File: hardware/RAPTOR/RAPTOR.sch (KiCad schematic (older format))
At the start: 45 parts, among them J1 SOLC_CONN, J2 SOLP_CONN, J3 JST_2MM_MALE, J4 CONN_LED_FIX, J5 CONN_SOLP_LED, J6 CONN_SOLC_LED, P1 Power, P2 Analog, P3 Digital, P4 Digital, P5 CONN_01X01, P6 CONN_01X01, P7 CONN_01X01, P8 CONN_01X01, Q1 MOSFET-NCH-2N7002PW, Q2 MOSFET-NCH-2N7002PW, Q3 MOSFET-NCH-2N7002PW, Q4 MOSFET-NCH-2N7002PW, SW1 EEPROM_BTN, SW2 SOLC_SW, SW3 SOLP_SW, U1 BMP280 Breakout, U2 BNO055 Breakout, U3 OpenLog, U4 AdafruitGPS, U5 U3V12F12, U6 L7805

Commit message: moved a single mosfet
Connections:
- wire segments 157 -> 158
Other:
- moved on the sheet: Q1
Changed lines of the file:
@@
 L RAPTOR-rescue:MOSFET-NCH-2N7002PW-SparkFun-DiscreteSemi Q1
 U 1 1 5BE8A581
-P 4850 2400
-F 0 "Q1" H 5015 2495 45  0000 L CNN
-F 1 "MOSFET-NCH-2N7002PW" H 5015 2411 45  0000 L CNN
-F 2 "SOT323" H 4850 2700 20  0001 C CNN
-F 3 "https://www.diodes.com/assets/Datasheets/ds11303.pdf" H 4850 2400 50  0001 C CNN
-F 4 "TRANS-11151" H 5015 2316 60  0000 L CNN "Field4"
-	1    4850 2400
-	1    0    0    -1
-$EndComp
-Text Label 4350 2500 0    50   ~ 0
+P 4850 2800
+F 0 "Q1" H 5015 2895 45  0000 L CNN
+F 1 "MOSFET-NCH-2N7002PW" H 5015 2811 45  0000 L CNN
+F 2 "SOT323" H 4850 3100 20  0001 C CNN
+F 3 "https://www.diodes.com/assets/Datasheets/ds11303.pdf" H 4850 2800 50  0001 C CNN
+F 4 "TRANS-11151" H 5015 2716 60  0000 L CNN "Field4"
+	1    4850 2800
+	1    0    0    -1
+$EndComp
+Text Label 4350 2900 0    50   ~ 0
 SOLP_DTA
 Wire Wire Line
-	4650 2500 4350 2500
+	4650 2900 4350 2900
 Wire Wire Line
 	4950 2100 4950 2200
@@
 L power:GND #PWR09
 U 1 1 5C3CAEEF
-P 4950 3000
-F 0 "#PWR09" H 4950 2750 50  0001 C CNN
-F 1 "GND" H 4955 2827 50  0000 C CNN
-F 2 "" H 4950 3000 50  0001 C CNN
-F 3 "" H 4950 3000 50  0001 C CNN
-	1    4950 3000
+P 4950 3100
+F 0 "#PWR09" H 4950 2850 50  0001 C CNN
+F 1 "GND" H 4955 2927 50  0000 C CNN
+F 2 "" H 4950 3100 50  0001 C CNN
+F 3 "" H 4950 3100 50  0001 C CNN
+	1    4950 3100
 	1    0    0    -1
 $EndComp
@@
 L SparkFun-DiscreteSemi:DIODE-1N4148 D9
 U 1 1 5C415339
-P 5850 2800
-F 0 "D9" V 5945 2722 45  0000 R CNN
-F 1 "DIODE-1N4148" V 5861 2722 45  0000 R CNN
-F 2 "DIODE-1N4148" H 5850 3000 20  0001 C CNN
-F 3 "" H 5850 2800 50  0001 C CNN
-F 4 "DIO-08378" V 5766 2722 60  0000 R CNN "Field4"
-	1    5850 2800
+P 5850 2400
+F 0 "D9" V 5945 2322 45  0000 R CNN
+F 1 "DIODE-1N4148" V 5861 2322 45  0000 R CNN
+F 2 "DIODE-1N4148" H 5850 2600 20  0001 C CNN
+F 3 "" H 5850 2400 50  0001 C CNN
+F 4 "DIO-08378" V 5766 2322 60  0000 R CNN "Field4"
+	1    5850 2400
 	0    -1   -1   0
 $EndComp
@@
 L SparkFun-Connectors:CONN_02 J2
 U 1 1 5C4D5A1A
-P 5050 2750
-F 0 "J2" H 4822 2705 45  0000 R CNN
-F 1 "SOLP_CONN" H 4822 2789 45  0000 R CNN
-F 2 "1X02" H 5050 3000 20  0001 C CNN
-F 3 "" H 5050 2750 50  0001 C CNN
-F 4 "XXX-00000" H 4822 2884 60  0000 R CNN "Field4"
-	1    5050 2750
+P 5050 2350
+F 0 "J2" H 4822 2305 45  0000 R CNN
+F 1 "SOLP_CONN" H 4822 2389 45  0000 R CNN
+F 2 "1X02" H 5050 2600 20  0001 C CNN
+F 3 "" H 5050 2350 50  0001 C CNN
+F 4 "XXX-00000" H 4822 2484 60  0000 R CNN "Field4"
+	1    5050 2350
 	-1   0    0    1
 $EndComp
 Wire Wire Line
-	4950 2600 4950 2750
-Wire Wire Line
-	4950 3000 4950 2850
-Wire Wire Line
-	4950 2600 5850 2600
-Wire Wire Line
-	5850 2600 5850 2700
-Connection ~ 4950 2600
-Wire Wire Line
-	5850 2900 5850 3000
-Wire Wire Line
-	5850 3000 4950 3000
-Connection ~ 4950 3000
+	4950 2200 4950 2350
+Wire Wire Line
+	4950 2600 4950 2450
+Wire Wire Line
+	4950 2200 5850 2200
+Wire Wire Line
+	5850 2200 5850 2300
+Wire Wire Line
+	5850 2500 5850 2600
+Wire Wire Line
+	5850 2600 4950 2600
 $Comp
 L power:+12V #PWR05
@@
 	1    0    0    -1
 $EndComp
+Connection ~ 4950 2200
+Connection ~ 4950 2600
+Wire Wire Line
+	4950 3000 4950 3100
 $EndSCHEMATC

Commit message: Fixed MOSFETS gate and drain on diagram
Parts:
- D8, D9: symbol SparkFun-DiscreteSemi:DIODE-1N4148 -> RAPTOR-rescue:DIODE-1N4148-SparkFun-DiscreteSemi
- J1, J2, J4, J5, J6: symbol SparkFun-Connectors:CONN_02 -> RAPTOR-rescue:CONN_02-SparkFun-Connectors
- J3: symbol SparkFun-Connectors:JST_2MM_MALE -> RAPTOR-rescue:JST_2MM_MALE-SparkFun-Connectors
- J? (x2): symbol SparkFun-Connectors:CONN_03 -> RAPTOR-rescue:CONN_03-SparkFun-Connectors
- R1, R2, R3, R4: symbol SparkFun-Resistors:150OHM-0603-1_10W-1% -> RAPTOR-rescue:150OHM-0603-1_10W-1%-SparkFun-Resistors
- R5, R6, R7: symbol SparkFun-Resistors:4.7KOHM-0603-1_10W-1% -> RAPTOR-rescue:4.7KOHM-0603-1_10W-1%-SparkFun-Resistors
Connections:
- wire segments 158 -> 163
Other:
- moved on the sheet: BZ1, D4, D5, D6, D7, Q2, Q3, Q4

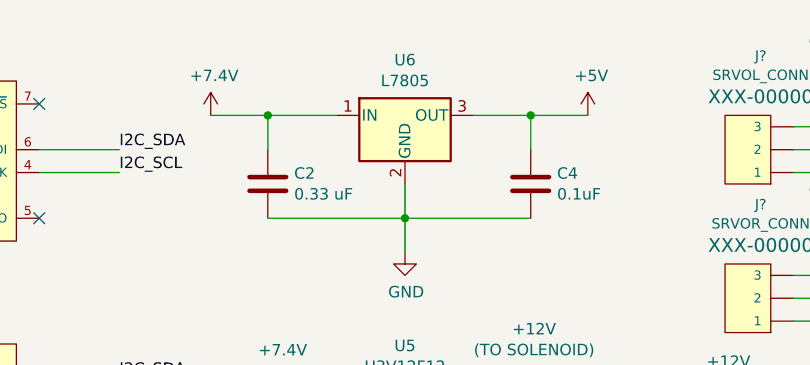
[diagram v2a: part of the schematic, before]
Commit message: change to L4940V5
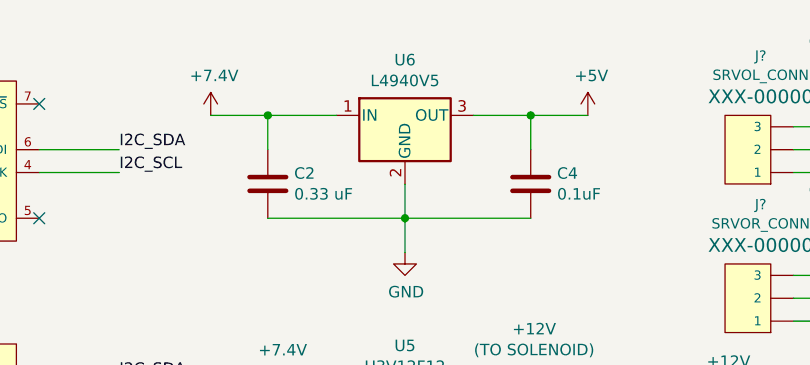
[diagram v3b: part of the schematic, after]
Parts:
- U6: value L7805 -> L4940V5
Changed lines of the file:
@@
-$EndComp
-$Comp
-L Regulator_Linear:L7805 U6
-U 1 1 5C49E003
-P 3550 850
-F 0 "U6" H 3550 1092 50  0000 C CNN
-F 1 "L7805" H 3550 1001 50  0000 C CNN
-F 2 "Package_TO_SOT_THT:TO-220-3_Horizontal_TabDown" H 3575 700 50  0001 L CIN
-F 3 "http://www.st.com/content/ccc/resource/technical/document/datasheet/41/4f/b3/b0/12/d4/47/88/CD00000444.pdf/files/CD00000444.pdf/jcr:content/translations/en.CD00000444.pdf" H 3550 800 50  0001 C CNN
-	1    3550 850
-	1    0    0    -1
 $EndComp
 $Comp
@@
 Wire Wire Line
 	1300 6950 1150 6950
+$Comp
+L Regulator_Linear:L7805 U6
+U 1 1 5C49E003
+P 3550 850
+F 0 "U6" H 3550 1092 50  0000 C CNN
+F 1 "L4940V5" H 3550 1001 50  0000 C CNN
+F 2 "Package_TO_SOT_THT:TO-220-3_Horizontal_TabDown" H 3575 700 50  0001 L CIN
+F 3 "http://www.st.com/content/ccc/resource/technical/document/datasheet/41/4f/b3/b0/12/d4/47/88/CD00000444.pdf/files/CD00000444.pdf/jcr:content/translations/en.CD00000444.pdf" H 3550 800 50  0001 C CNN
+	1    3550 850
+	1    0    0    -1
+$EndComp
 $EndSCHEMATC

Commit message: change LED resistor values
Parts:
- removed R1, R2, R3, R4: 150OHM-0603-1_10W-1%, 0603, symbol RAPTOR-rescue:150OHM-0603-1_10W-1%-SparkFun-Resistors
- added R? (x3): 100OHM-0603-1_10W-1%, 0603, symbol SparkFun-Resistors:100OHM-0603-1_10W-1%
- added R?: 20OHM-0603-1_10W-1%, 0603, symbol SparkFun-Resistors:20OHM-0603-1_10W-1%
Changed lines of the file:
@@
 Wire Wire Line
 	3250 3200 3250 3400
-$Comp
-L RAPTOR-rescue:150OHM-0603-1_10W-1%-SparkFun-Resistors R2
-U 1 1 5C41D14D
-P 6000 5200
-F 0 "R2" H 6000 5500 45  0000 C CNN
-F 1 "150OHM-0603-1_10W-1%" H 6000 5416 45  0000 C CNN
-F 2 "0603" H 6000 5350 20  0001 C CNN
-F 3 "" H 6000 5200 60  0001 C CNN
-F 4 "RES-11028" H 6000 5321 60  0000 C CNN "Field4"
-	1    6000 5200
-	1    0    0    -1
-$EndComp
 Wire Wire Line
 	6200 5200 6450 5200
-$Comp
-L RAPTOR-rescue:150OHM-0603-1_10W-1%-SparkFun-Resistors R1
-U 1 1 5C49189B
-P 1600 5700
-F 0 "R1" V 1505 5768 45  0000 L CNN
-F 1 "150OHM-0603-1_10W-1%" V 1589 5768 45  0000 L CNN
-F 2 "0603" H 1600 5850 20  0001 C CNN
-F 3 "" H 1600 5700 60  0001 C CNN
-F 4 "RES-11028" V 1684 5768 60  0000 L CNN "Field4"
-	1    1600 5700
-	0    1    1    0
-$EndComp
 $Comp
 L Switch:SW_SPST SW1
@@
 Wire Wire Line
 	4600 5950 4600 6050
-$Comp
-L RAPTOR-rescue:150OHM-0603-1_10W-1%-SparkFun-Resistors R3
-U 1 1 5C5D41D4
-P 6000 5950
-F 0 "R3" H 6000 6250 45  0000 C CNN
-F 1 "150OHM-0603-1_10W-1%" H 6000 6166 45  0000 C CNN
-F 2 "0603" H 6000 6100 20  0001 C CNN
-F 3 "" H 6000 5950 60  0001 C CNN
-F 4 "RES-11028" H 6000 6071 60  0000 C CNN "Field4"
-	1    6000 5950
-	1    0    0    -1
-$EndComp
 Wire Wire Line
 	6200 5950 6450 5950
@@
 Wire Wire Line
 	4600 6650 4600 6750
-$Comp
-L RAPTOR-rescue:150OHM-0603-1_10W-1%-SparkFun-Resistors R4
-U 1 1 5C5E257E
-P 6000 6650
-F 0 "R4" H 6000 6950 45  0000 C CNN
-F 1 "150OHM-0603-1_10W-1%" H 6000 6866 45  0000 C CNN
-F 2 "0603" H 6000 6800 20  0001 C CNN
-F 3 "" H 6000 6650 60  0001 C CNN
-F 4 "RES-11028" H 6000 6771 60  0000 C CNN "Field4"
-	1    6000 6650
-	1    0    0    -1
-$EndComp
 Wire Wire Line
 	6200 6650 6450 6650
@@
 	1    0    0    -1
 $EndComp
+$Comp
+L SparkFun-Resistors:100OHM-0603-1_10W-1% R?
+U 1 1 5C409EAA
+P 6000 6650
+F 0 "R?" H 6000 6950 45  0000 C CNN
+F 1 "100OHM-0603-1_10W-1%" H 6000 6866 45  0000 C CNN
+F 2 "0603" H 6000 6800 20  0001 C CNN
+F 3 "" H 6000 6650 60  0001 C CNN
+F 4 "RES-07863" H 6000 6771 60  0000 C CNN "Field4"
+	1    6000 6650
+	1    0    0    -1
+$EndComp
+$Comp
+L SparkFun-Resistors:100OHM-0603-1_10W-1% R?
+U 1 1 5C409F6D
+P 6000 5950
+F 0 "R?" H 6000 6250 45  0000 C CNN
+F 1 "100OHM-0603-1_10W-1%" H 6000 6166 45  0000 C CNN
+F 2 "0603" H 6000 6100 20  0001 C CNN
+F 3 "" H 6000 5950 60  0001 C CNN
+F 4 "RES-07863" H 6000 6071 60  0000 C CNN "Field4"
+	1    6000 5950
+	1    0    0    -1
+$EndComp
+$Comp
+L SparkFun-Resistors:100OHM-0603-1_10W-1% R?
+U 1 1 5C411D44
+P 6000 5200
+F 0 "R?" H 6000 5500 45  0000 C CNN
+F 1 "100OHM-0603-1_10W-1%" H 6000 5416 45  0000 C CNN
+F 2 "0603" H 6000 5350 20  0001 C CNN
+F 3 "" H 6000 5200 60  0001 C CNN
+F 4 "RES-07863" H 6000 5321 60  0000 C CNN "Field4"
+	1    6000 5200
+	1    0    0    -1
+$EndComp
+$Comp
+L SparkFun-Resistors:20OHM-0603-1_10W-1% R?
+U 1 1 5C41AD57
+P 1600 5700
+F 0 "R?" V 1505 5768 45  0000 L CNN
+F 1 "20OHM-0603-1_10W-1%" V 1589 5768 45  0000 L CNN
+F 2 "0603" H 1600 5850 20  0001 C CNN
+F 3 "" H 1600 5700 60  0001 C CNN
+F 4 "RES-07862" V 1684 5768 60  0000 L CNN "Field4"
+	1    1600 5700
+	0    1    1    0
+$EndComp
 $EndSCHEMATC

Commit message: add a hotwire
Needs correct labeling
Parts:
- added Q?: MOSFET-NCH-2N7002PW, SOT323, symbol RAPTOR-rescue:MOSFET-NCH-2N7002PW-SparkFun-DiscreteSemi
- R? (x3): symbol SparkFun-Resistors:100OHM-0603-1_10W-1% -> RAPTOR-rescue:100OHM-0603-1_10W-1%-SparkFun-Resistors
- R?: symbol SparkFun-Resistors:20OHM-0603-1_10W-1% -> RAPTOR-rescue:20OHM-0603-1_10W-1%-SparkFun-Resistors
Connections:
- net labels added: HOTWIRE, PWR_HOTWIRE
- wire segments 163 -> 165
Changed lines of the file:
@@
 $EndComp
 $Comp
-L SparkFun-Resistors:100OHM-0603-1_10W-1% R?
+L RAPTOR-rescue:100OHM-0603-1_10W-1%-SparkFun-Resistors R?
 U 1 1 5C409EAA
 P 6000 6650
@@
 $EndComp
 $Comp
-L SparkFun-Resistors:100OHM-0603-1_10W-1% R?
+L RAPTOR-rescue:100OHM-0603-1_10W-1%-SparkFun-Resistors R?
 U 1 1 5C409F6D
 P 6000 5950
@@
 $EndComp
 $Comp
-L SparkFun-Resistors:100OHM-0603-1_10W-1% R?
+L RAPTOR-rescue:100OHM-0603-1_10W-1%-SparkFun-Resistors R?
 U 1 1 5C411D44
 P 6000 5200
@@
 $EndComp
 $Comp
-L SparkFun-Resistors:20OHM-0603-1_10W-1% R?
+L RAPTOR-rescue:20OHM-0603-1_10W-1%-SparkFun-Resistors R?
 U 1 1 5C41AD57
 P 1600 5700
@@
 	0    1    1    0
 $EndComp
+$Comp
+L RAPTOR-rescue:MOSFET-NCH-2N7002PW-SparkFun-DiscreteSemi Q?
+U 1 1 5C4073ED
+P 7200 3050
+F 0 "Q?" H 7365 3145 45  0000 L CNN
+F 1 "MOSFET-NCH-2N7002PW" H 7365 3061 45  0000 L CNN
+F 2 "SOT323" H 7200 3350 20  0001 C CNN
+F 3 "https://www.diodes.com/assets/Datasheets/ds11303.pdf" H 7200 3050 50  0001 C CNN
+F 4 "TRANS-11151" H 7365 2966 60  0000 L CNN "Field4"
+	1    7200 3050
+	1    0    0    -1
+$EndComp
+$Comp
+L power:GND #PWR?
+U 1 1 5C417257
+P 7300 3350
+F 0 "#PWR?" H 7300 3100 50  0001 C CNN
+F 1 "GND" H 7305 3177 50  0000 C CNN
+F 2 "" H 7300 3350 50  0001 C CNN
+F 3 "" H 7300 3350 50  0001 C CNN
+	1    7300 3350
+	1    0    0    -1
+$EndComp
+Wire Wire Line
+	7300 3250 7300 3350
+Wire Wire Line
+	7300 2850 7300 2400
+Text Label 7000 3150 2    50   ~ 0
+HOTWIRE
+Text Label 7300 2400 2    50   ~ 0
+PWR_HOTWIRE
 $EndSCHEMATC

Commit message: fix hotwire
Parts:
- removed Q?: MOSFET-NCH-2N7002PW, SOT323, symbol RAPTOR-rescue:MOSFET-NCH-2N7002PW-SparkFun-DiscreteSemi
- added J?: HOTWIRE_CONN, 1X02, symbol RAPTOR-rescue:CONN_02-SparkFun-Connectors
- added Q?: MOSFET-NCH-2N7002PW, SOT323, symbol RAPTOR-rescue:MOSFET-NCH-2N7002PW-SparkFun-DiscreteSemi
- added R?: 4.7KOHM-0603-1_10W-1%, 0603, symbol RAPTOR-rescue:4.7KOHM-0603-1_10W-1%-SparkFun-Resistors
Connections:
- net +7.5V: now also J?.1
- net GND: now also R?.2
- net HOTWIRE: now also P4.4, Q?.1 (G)
- new net: Q?.2 (S), R?.1
- new net: J?.2, Q?.3 (D)
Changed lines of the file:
@@
 $Comp
 L RAPTOR-rescue:MOSFET-NCH-2N7002PW-SparkFun-DiscreteSemi Q?
-U 1 1 5C4073ED
-P 7200 3050
-F 0 "Q?" H 7365 3145 45  0000 L CNN
-F 1 "MOSFET-NCH-2N7002PW" H 7365 3061 45  0000 L CNN
-F 2 "SOT323" H 7200 3350 20  0001 C CNN
-F 3 "https://www.diodes.com/assets/Datasheets/ds11303.pdf" H 7200 3050 50  0001 C CNN
-F 4 "TRANS-11151" H 7365 2966 60  0000 L CNN "Field4"
-	1    7200 3050
+U 1 1 5C45C6C5
+P 7150 3150
+F 0 "Q?" H 7315 3245 45  0000 L CNN
+F 1 "MOSFET-NCH-2N7002PW" H 7315 3161 45  0000 L CNN
+F 2 "SOT323" H 7150 3450 20  0001 C CNN
+F 3 "https://www.diodes.com/assets/Datasheets/ds11303.pdf" H 7150 3150 50  0001 C CNN
+F 4 "TRANS-11151" H 7315 3066 60  0000 L CNN "Field4"
+	1    7150 3150
+	1    0    0    -1
+$EndComp
+Text Label 6650 3250 0    50   ~ 0
+HOTWIRE
+Wire Wire Line
+	6950 3250 6650 3250
+$Comp
+L power:GND #PWR?
+U 1 1 5C45C6CF
+P 7250 3850
+F 0 "#PWR?" H 7250 3600 50  0001 C CNN
+F 1 "GND" H 7255 3677 50  0000 C CNN
+F 2 "" H 7250 3850 50  0001 C CNN
+F 3 "" H 7250 3850 50  0001 C CNN
+	1    7250 3850
 	1    0    0    -1
 $EndComp
 $Comp
-L power:GND #PWR?
-U 1 1 5C417257
-P 7300 3350
-F 0 "#PWR?" H 7300 3100 50  0001 C CNN
-F 1 "GND" H 7305 3177 50  0000 C CNN
-F 2 "" H 7300 3350 50  0001 C CNN
-F 3 "" H 7300 3350 50  0001 C CNN
-	1    7300 3350
+L RAPTOR-rescue:CONN_02-SparkFun-Connectors J?
+U 1 1 5C45C6DE
+P 7350 2700
+F 0 "J?" H 7122 2655 45  0000 R CNN
+F 1 "HOTWIRE_CONN" H 7122 2739 45  0000 R CNN
+F 2 "1X02" H 7350 2950 20  0001 C CNN
+F 3 "" H 7350 2700 50  0001 C CNN
+F 4 "XXX-00000" H 7122 2834 60  0000 R CNN "Field4"
+	1    7350 2700
+	-1   0    0    1
+$EndComp
+Wire Wire Line
+	7250 2950 7250 2800
+Text Label 10550 2600 0    50   ~ 0
+HOTWIRE
+$Comp
+L RAPTOR-rescue:4.7KOHM-0603-1_10W-1%-SparkFun-Resistors R?
+U 1 1 5C476CBF
+P 7250 3600
+F 0 "R?" V 7155 3668 45  0000 L CNN
+F 1 "4.7KOHM-0603-1_10W-1%" V 7239 3668 45  0000 L CNN
+F 2 "0603" H 7250 3750 20  0001 C CNN
+F 3 "" H 7250 3600 60  0001 C CNN
+F 4 "RES-07857" V 7334 3668 60  0000 L CNN "Field4"
+	1    7250 3600
+	0    1    1    0
+$EndComp
+Wire Wire Line
+	7250 3350 7250 3400
+Wire Wire Line
+	7250 3800 7250 3850
+Wire Wire Line
+	7250 2450 7250 2700
+$Comp
+L power:+7.5V #PWR?
+U 1 1 5C4B44D8
+P 7250 2450
+F 0 "#PWR?" H 7250 2300 50  0001 C CNN
+F 1 "+7.5V" H 7265 2623 50  0001 C CNN
+F 2 "" H 7250 2450 50  0001 C CNN
+F 3 "" H 7250 2450 50  0001 C CNN
+F 4 "+7.4V" H 7265 2623 50  0000 C CNN "Real Value"
+	1    7250 2450
 	1    0    0    -1
 $EndComp
-Wire Wire Line
-	7300 3250 7300 3350
-Wire Wire Line
-	7300 2850 7300 2400
-Text Label 7000 3150 2    50   ~ 0
-HOTWIRE
-Text Label 7300 2400 2    50   ~ 0
-PWR_HOTWIRE
 $EndSCHEMATC

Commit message: add RBF
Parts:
- added SW?: RBF, symbol Switch:SW_SPST
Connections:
- net +7.5V: now also SW?.2 (B); no longer J3.2 (+)
- new net: J3.2 (+), SW?.1 (A)
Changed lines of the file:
@@
 L power:+7.5V #PWR015
 U 1 1 5C4F2CBE
-P 3550 3050
-F 0 "#PWR015" H 3550 2900 50  0001 C CNN
-F 1 "+7.5V" H 3565 3223 50  0001 C CNN
-F 2 "" H 3550 3050 50  0001 C CNN
-F 3 "" H 3550 3050 50  0001 C CNN
-F 4 "+7.4V" H 3565 3223 50  0000 C CNN "Real Value"
-	1    3550 3050
-	1    0    0    -1
-$EndComp
-Wire Wire Line
-	3550 3050 3550 3200
+P 3950 3050
+F 0 "#PWR015" H 3950 2900 50  0001 C CNN
+F 1 "+7.5V" H 3965 3223 50  0001 C CNN
+F 2 "" H 3950 3050 50  0001 C CNN
+F 3 "" H 3950 3050 50  0001 C CNN
+F 4 "+7.4V" H 3965 3223 50  0000 C CNN "Real Value"
+	1    3950 3050
+	1    0    0    -1
+$EndComp
+Wire Wire Line
+	3950 3050 3950 3200
 $Comp
 L power:GND #PWR09
@@
 	3550 3700 3550 3800
 Wire Wire Line
-	3550 3200 3250 3200
-Wire Wire Line
 	3250 3200 3250 3400
 Wire Wire Line
@@
 	1    0    0    -1
 $EndComp
+$Comp
+L Switch:SW_SPST SW?
+U 1 1 5C4BDD6E
+P 3600 3200
+F 0 "SW?" H 3600 3435 50  0000 C CNN
+F 1 "RBF" H 3600 3344 50  0000 C CNN
+F 2 "" H 3600 3200 50  0001 C CNN
+F 3 "" H 3600 3200 50  0001 C CNN
+	1    3600 3200
+	1    0    0    -1
+$EndComp
+Wire Wire Line
+	3250 3200 3400 3200
+Wire Wire Line
+	3800 3200 3950 3200
 $EndSCHEMATC
